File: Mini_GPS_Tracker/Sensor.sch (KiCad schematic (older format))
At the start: 15 parts

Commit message: added stm core connections
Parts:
- C14, C15, C16, C17, C18, C5, C8: renamed from C?; footprint (none) -> Capacitor_SMD:C_0805_2012Metric_Pad1.15x1.40mm_HandSolder
- R4, R5, R8: renamed from R?; footprint (none) -> Resistor_SMD:R_0805_2012Metric_Pad1.15x1.40mm_HandSolder
- Y2: renamed from Y?; footprint (none) -> Crystal:Crystal_SMD_2012-2Pin_2.0x1.2mm_HandSoldering
- gave numbers to parts that had none: 4
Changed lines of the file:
@@
 $EndDescr
 $Comp
-L Sensor_Motion:BNO055 U?
+L Sensor_Motion:BNO055 U7
 U 1 1 5E8555C8
 P 7700 3550
-F 0 "U?" H 7700 4431 50  0000 C CNN
+F 0 "U7" H 7700 4431 50  0000 C CNN
 F 1 "BNO055" H 7700 4340 50  0000 C CNN
 F 2 "Package_LGA:LGA-28_5.2x3.8mm_P0.5mm" H 7950 2900 50  0001 L CNN
@@
 	2500 6700 2500 6850
 $Comp
-L pspice:CAP C?
+L pspice:CAP C3
 U 1 1 5E6E943F
 P 3650 6350
-F 0 "C?" H 3828 6396 50  0000 L CNN
+F 0 "C3" H 3828 6396 50  0000 L CNN
 F 1 "100nF" H 3828 6305 50  0000 L CNN
 F 2 "Capacitor_SMD:C_0805_2012Metric_Pad1.15x1.40mm_HandSolder" H 3650 6350 50  0001 C CNN
@@
 $EndComp
 $Comp
-L power:+3.3V #PWR?
+L power:+3.3V #PWR0101
 U 1 1 5E6E8AC2
 P 2500 5550
-F 0 "#PWR?" H 2500 5400 50  0001 C CNN
+F 0 "#PWR0101" H 2500 5400 50  0001 C CNN
 F 1 "+3.3V" H 2515 5723 50  0000 C CNN
 F 2 "" H 2500 5550 50  0001 C CNN
@@
 $EndComp
 $Comp
-L power:GND #PWR?
+L power:GND #PWR0102
 U 1 1 5E6E7BFC
 P 2500 6950
-F 0 "#PWR?" H 2500 6700 50  0001 C CNN
+F 0 "#PWR0102" H 2500 6700 50  0001 C CNN
 F 1 "GND" H 2505 6777 50  0000 C CNN
 F 2 "" H 2500 6950 50  0001 C CNN
@@
 	1700 6400 2100 6400
 $Comp
-L Sensor_Pressure:MS5611-01BA U?
+L Sensor_Pressure:MS5611-01BA U2
 U 1 1 5E6E6D79
 P 2500 6300
-F 0 "U?" H 2830 6346 50  0000 L CNN
+F 0 "U2" H 2830 6346 50  0000 L CNN
 F 1 "MS5611-01BA" H 2830 6255 50  0000 L CNN
 F 2 "Package_LGA:LGA-8_3x5mm_P1.25mm" H 2500 6300 50  0001 C CNN
@@
 $EndComp
 $Comp
-L Sensor_Motion:ADXL343 U?
+L Sensor_Motion:ADXL343 U1
 U 1 1 5E8940BD
 P 2500 1950
-F 0 "U?" H 3044 1996 50  0000 L CNN
+F 0 "U1" H 3044 1996 50  0000 L CNN
 F 1 "ADXL343" H 3044 1905 50  0000 L CNN
 F 2 "Package_LGA:LGA-14_3x5mm_P0.8mm_LayoutBorder1x6y" H 2500 1950 50  0001 C CNN
@@
 $EndComp
 $Comp
-L power:GND #PWR?
+L power:GND #PWR0117
 U 1 1 5E8951BC
 P 2500 2950
-F 0 "#PWR?" H 2500 2700 50  0001 C CNN
+F 0 "#PWR0117" H 2500 2700 50  0001 C CNN
 F 1 "GND" H 2505 2777 50  0000 C CNN
 F 2 "" H 2500 2950 50  0001 C CNN
@@
 	1450 1850 2000 1850
 $Comp
-L pspice:CAP C?
+L pspice:CAP C5
 U 1 1 5E89F2A3
 P 3700 1950
-F 0 "C?" H 3878 1996 50  0000 L CNN
+F 0 "C5" H 3878 1996 50  0000 L CNN
 F 1 "0.1uF" H 3878 1905 50  0000 L CNN
-F 2 "" H 3700 1950 50  0001 C CNN
+F 2 "Capacitor_SMD:C_0805_2012Metric_Pad1.15x1.40mm_HandSolder" H 3700 1950 50  0001 C CNN
 F 3 "~" H 3700 1950 50  0001 C CNN
 	1    3700 1950
@@
 $EndComp
 $Comp
-L pspice:CAP C?
+L pspice:CAP C8
 U 1 1 5E89F917
 P 4200 1950
-F 0 "C?" H 4378 1996 50  0000 L CNN
+F 0 "C8" H 4378 1996 50  0000 L CNN
 F 1 "0.1uF" H 4378 1905 50  0000 L CNN
-F 2 "" H 4200 1950 50  0001 C CNN
+F 2 "Capacitor_SMD:C_0805_2012Metric_Pad1.15x1.40mm_HandSolder" H 4200 1950 50  0001 C CNN
 F 3 "~" H 4200 1950 50  0001 C CNN
 	1    4200 1950
@@
 	2500 2550 2500 2800
 $Comp
-L pspice:CAP C?
+L pspice:CAP C14
 U 1 1 5E8A3F23
 P 4700 1950
-F 0 "C?" H 4878 1996 50  0000 L CNN
+F 0 "C14" H 4878 1996 50  0000 L CNN
 F 1 "10uF" H 4878 1905 50  0000 L CNN
-F 2 "" H 4700 1950 50  0001 C CNN
+F 2 "Capacitor_SMD:C_0805_2012Metric_Pad1.15x1.40mm_HandSolder" H 4700 1950 50  0001 C CNN
 F 3 "~" H 4700 1950 50  0001 C CNN
 	1    4700 1950
@@
 NoConn ~ 2700 2450
 $Comp
-L power:GND #PWR?
+L power:GND #PWR0118
 U 1 1 5E8806F6
 P 7600 4550
-F 0 "#PWR?" H 7600 4300 50  0001 C CNN
+F 0 "#PWR0118" H 7600 4300 50  0001 C CNN
 F 1 "GND" H 7605 4377 50  0000 C CNN
 F 2 "" H 7600 4550 50  0001 C CNN
@@
 $EndComp
 $Comp
-L power:+3.3V #PWR?
+L power:+3.3V #PWR0119
 U 1 1 5E88107E
 P 7600 2350
-F 0 "#PWR?" H 7600 2200 50  0001 C CNN
+F 0 "#PWR0119" H 7600 2200 50  0001 C CNN
 F 1 "+3.3V" H 7615 2523 50  0000 C CNN
 F 2 "" H 7600 2350 50  0001 C CNN
@@
 	7600 2650 7600 2850
 $Comp
-L Device:Crystal Y?
+L Device:Crystal Y2
 U 1 1 5E883E67
 P 8600 3250
-F 0 "Y?" V 8554 3381 50  0000 L CNN
+F 0 "Y2" V 8554 3381 50  0000 L CNN
 F 1 "32.7568KHz" V 8645 3381 50  0000 L CNN
-F 2 "" H 8600 3250 50  0001 C CNN
+F 2 "Crystal:Crystal_SMD_2012-2Pin_2.0x1.2mm_HandSoldering" H 8600 3250 50  0001 C CNN
 F 3 "~" H 8600 3250 50  0001 C CNN
 	1    8600 3250
@@
 $EndComp
 $Comp
-L pspice:CAP C?
+L pspice:CAP C17
 U 1 1 5E884BB2
 P 9300 3050
-F 0 "C?" V 9615 3050 50  0000 C CNN
+F 0 "C17" V 9615 3050 50  0000 C CNN
 F 1 "22pF" V 9524 3050 50  0000 C CNN
-F 2 "" H 9300 3050 50  0001 C CNN
+F 2 "Capacitor_SMD:C_0805_2012Metric_Pad1.15x1.40mm_HandSolder" H 9300 3050 50  0001 C CNN
 F 3 "~" H 9300 3050 50  0001 C CNN
 	1    9300 3050
@@
 $EndComp
 $Comp
-L pspice:CAP C?
+L pspice:CAP C18
 U 1 1 5E886F55
 P 9300 3550
-F 0 "C?" V 8985 3550 50  0000 C CNN
+F 0 "C18" V 8985 3550 50  0000 C CNN
 F 1 "22pF" V 9076 3550 50  0000 C CNN
-F 2 "" H 9300 3550 50  0001 C CNN
+F 2 "Capacitor_SMD:C_0805_2012Metric_Pad1.15x1.40mm_HandSolder" H 9300 3550 50  0001 C CNN
 F 3 "~" H 9300 3550 50  0001 C CNN
 	1    9300 3550
@@
 $EndComp
 $Comp
-L power:GND #PWR?
+L power:GND #PWR0120
 U 1 1 5E8880AB
 P 9850 3300
-F 0 "#PWR?" H 9850 3050 50  0001 C CNN
+F 0 "#PWR0120" H 9850 3050 50  0001 C CNN
 F 1 "GND" H 9855 3127 50  0000 C CNN
 F 2 "" H 9850 3300 50  0001 C CNN
@@
 	8600 3050 9050 3050
 $Comp
-L power:GND #PWR?
+L power:GND #PWR0121
 U 1 1 5E88DCA8
 P 7000 2450
-F 0 "#PWR?" H 7000 2200 50  0001 C CNN
+F 0 "#PWR0121" H 7000 2200 50  0001 C CNN
 F 1 "GND" V 7005 2322 50  0000 R CNN
 F 2 "" H 7000 2450 50  0001 C CNN
@@
 $EndComp
 $Comp
-L pspice:CAP C?
+L pspice:CAP C15
 U 1 1 5E88E6A0
 P 7350 2450
-F 0 "C?" V 7035 2450 50  0000 C CNN
+F 0 "C15" V 7035 2450 50  0000 C CNN
 F 1 "0.1uF" V 7126 2450 50  0000 C CNN
-F 2 "" H 7350 2450 50  0001 C CNN
+F 2 "Capacitor_SMD:C_0805_2012Metric_Pad1.15x1.40mm_HandSolder" H 7350 2450 50  0001 C CNN
 F 3 "~" H 7350 2450 50  0001 C CNN
 	1    7350 2450
@@
 	7000 2450 7100 2450
 $Comp
-L Device:R R?
+L Device:R R5
 U 1 1 5E892309
 P 8650 3850
-F 0 "R?" V 8857 3850 50  0000 C CNN
+F 0 "R5" V 8857 3850 50  0000 C CNN
 F 1 "10k" V 8766 3850 50  0000 C CNN
-F 2 "" V 8580 3850 50  0001 C CNN
+F 2 "Resistor_SMD:R_0805_2012Metric_Pad1.15x1.40mm_HandSolder" V 8580 3850 50  0001 C CNN
 F 3 "~" H 8650 3850 50  0001 C CNN
 	1    8650 3850
@@
 $EndComp
 $Comp
-L Device:R R?
+L Device:R R8
 U 1 1 5E892CDB
 P 9150 3950
-F 0 "R?" V 8943 3950 50  0000 C CNN
+F 0 "R8" V 8943 3950 50  0000 C CNN
 F 1 "10k" V 9034 3950 50  0000 C CNN
-F 2 "" V 9080 3950 50  0001 C CNN
+F 2 "Resistor_SMD:R_0805_2012Metric_Pad1.15x1.40mm_HandSolder" V 9080 3950 50  0001 C CNN
 F 3 "~" H 9150 3950 50  0001 C CNN
 	1    9150 3950
@@
 $EndComp
 $Comp
-L power:GND #PWR?
+L power:GND #PWR0122
 U 1 1 5E8937EF
 P 9950 3850
-F 0 "#PWR?" H 9950 3600 50  0001 C CNN
+F 0 "#PWR0122" H 9950 3600 50  0001 C CNN
 F 1 "GND" V 9955 3722 50  0000 R CNN
 F 2 "" H 9950 3850 50  0001 C CNN
@@
 $EndComp
 $Comp
-L power:GND #PWR?
+L power:GND #PWR0123
 U 1 1 5E894898
 P 9950 3950
-F 0 "#PWR?" H 9950 3700 50  0001 C CNN
+F 0 "#PWR0123" H 9950 3700 50  0001 C CNN
 F 1 "GND" V 9955 3822 50  0000 R CNN
 F 2 "" H 9950 3950 50  0001 C CNN
@@
 $EndComp
 $Comp
-L pspice:CAP C?
+L pspice:CAP C16
 U 1 1 5E8959B0
 P 8550 4450
-F 0 "C?" V 8235 4450 50  0000 C CNN
+F 0 "C16" V 8235 4450 50  0000 C CNN
 F 1 "0.1uF" V 8326 4450 50  0000 C CNN
-F 2 "" H 8550 4450 50  0001 C CNN
+F 2 "Capacitor_SMD:C_0805_2012Metric_Pad1.15x1.40mm_HandSolder" H 8550 4450 50  0001 C CNN
 F 3 "~" H 8550 4450 50  0001 C CNN
 	1    8550 4450
@@
 $EndComp
 $Comp
-L power:GND #PWR?
+L power:GND #PWR0124
 U 1 1 5E89C6D8
 P 8550 4800
-F 0 "#PWR?" H 8550 4550 50  0001 C CNN
+F 0 "#PWR0124" H 8550 4550 50  0001 C CNN
 F 1 "GND" V 8555 4672 50  0000 R CNN
 F 2 "" H 8550 4800 50  0001 C CNN
@@
 	8550 4050 8550 4200
 $Comp
-L Device:R R?
+L Device:R R4
 U 1 1 5E897EFC
 P 6950 4300
-F 0 "R?" H 7020 4346 50  0000 L CNN
+F 0 "R4" H 7020 4346 50  0000 L CNN
 F 1 "10K" H 7020 4255 50  0000 L CNN
-F 2 "" V 6880 4300 50  0001 C CNN
+F 2 "Resistor_SMD:R_0805_2012Metric_Pad1.15x1.40mm_HandSolder" V 6880 4300 50  0001 C CNN
 F 3 "~" H 6950 4300 50  0001 C CNN
 	1    6950 4300
@@
 $EndComp
 $Comp
-L power:GND #PWR?
+L power:GND #PWR0125
 U 1 1 5E898E99
 P 6950 4550
-F 0 "#PWR?" H 6950 4300 50  0001 C CNN
+F 0 "#PWR0125" H 6950 4300 50  0001 C CNN
 F 1 "GND" H 6955 4377 50  0000 C CNN
 F 2 "" H 6950 4550 50  0001 C CNN
@@
 $EndComp
 $Comp
-L power:GND #PWR?
+L power:GND #PWR0126
 U 1 1 5E89968D
 P 6600 4550
-F 0 "#PWR?" H 6600 4300 50  0001 C CNN
+F 0 "#PWR0126" H 6600 4300 50  0001 C CNN
 F 1 "GND" H 6605 4377 50  0000 C CNN
 F 2 "" H 6600 4550 50  0001 C CNN
@@
 	6550 3850 7100 3850
 $Comp
-L power:GND #PWR?
+L power:GND #PWR0127
 U 1 1 5E8A27A4
 P 5500 3550
-F 0 "#PWR?" H 5500 3300 50  0001 C CNN
+F 0 "#PWR0127" H 5500 3300 50  0001 C CNN
 F 1 "GND" H 5505 3377 50  0000 C CNN
 F 2 "" H 5500 3550 50  0001 C CNN
@@
 $EndComp
 $Comp
-L power:+3.3V #PWR?
+L power:+3.3V #PWR0128
 U 1 1 5E8A32E9
 P 5500 3450
-F 0 "#PWR?" H 5500 3300 50  0001 C CNN
+F 0 "#PWR0128" H 5500 3300 50  0001 C CNN
 F 1 "+3.3V" H 5515 3623 50  0000 C CNN
 F 2 "" H 5500 3450 50  0001 C CNN

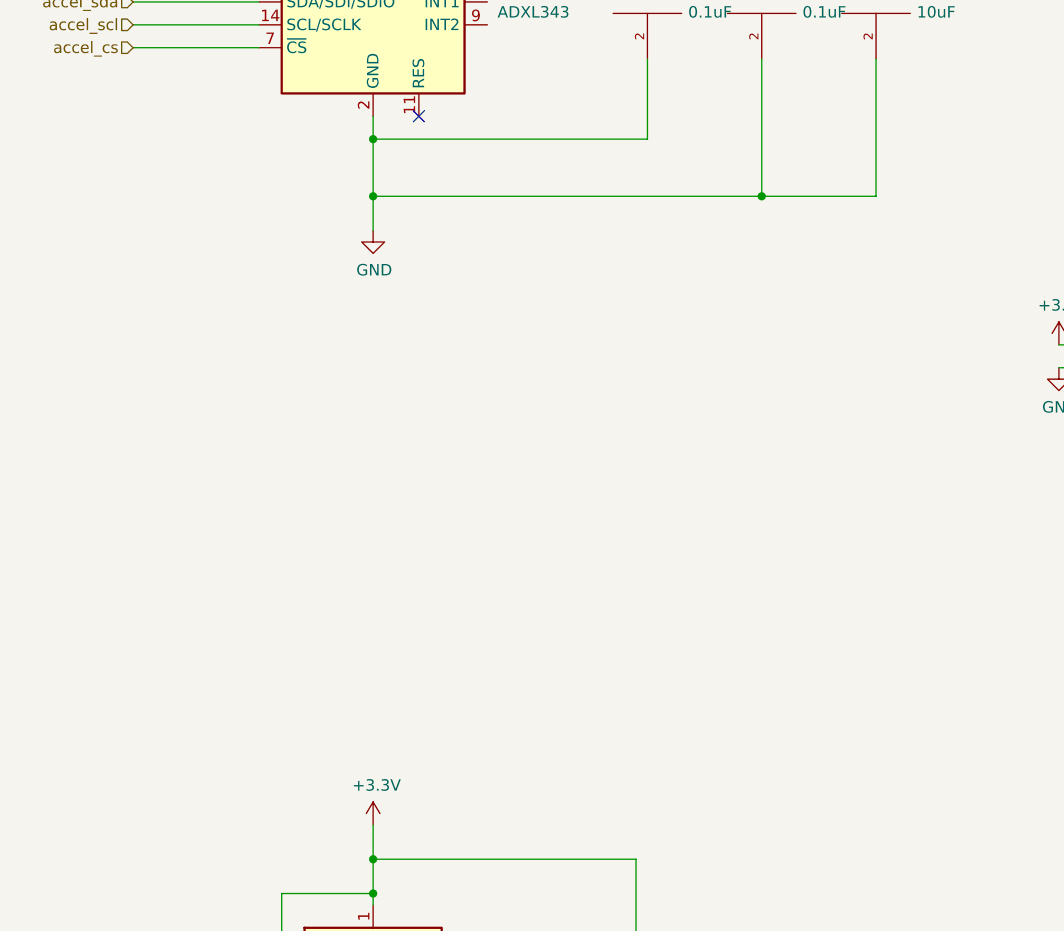
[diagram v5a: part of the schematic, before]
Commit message: Add files via upload
Making update for 100 pin CPU
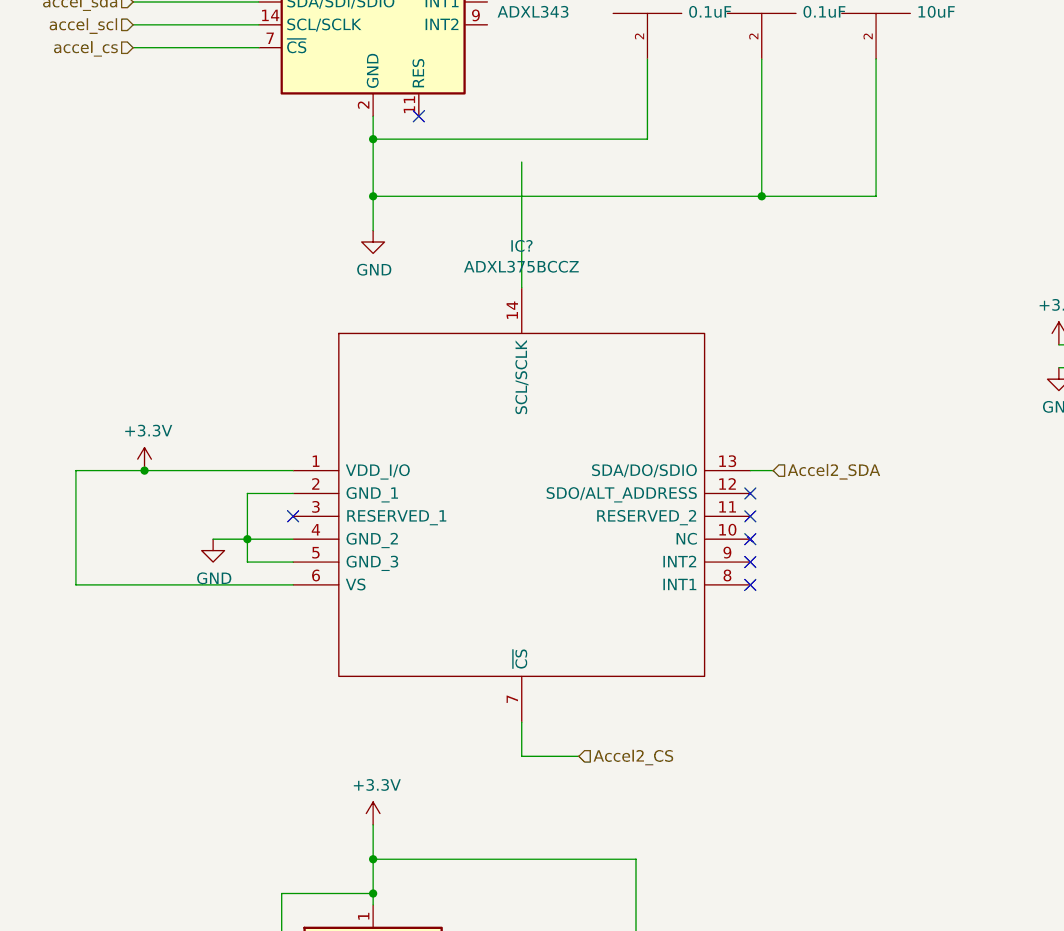
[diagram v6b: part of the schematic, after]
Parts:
- added IC?: ADXL375BCCZ, CC-14-1, symbol SamacSys_Parts:ADXL375BCCZ
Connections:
- net +3V3: now also IC?.1 (VDD_I/O), IC?.6 (VS)
- net GND: now also IC?.2 (GND_1), IC?.4 (GND_2), IC?.5 (GND_3)
- new net Accel2_CS: IC?.7 (~CS)
- new net Accel2_SDA: IC?.13 (SDA/DO/SDIO)
- no-connect marks 4 -> 10
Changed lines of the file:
@@
 EESchema Schematic File Version 4
+LIBS:Mini_GPS_Tracker-cache
 EELAYER 30 0
 EELAYER END
 $Descr A4 11693 8268
 encoding utf-8
-Sheet 2 11
+Sheet 2 7
 Title ""
 Date ""
@@
 Wire Wire Line
 	7100 3550 5500 3550
+Text HLabel 4250 4000 2    50   Input ~ 0
+Accel2_SDA
+Wire Wire Line
+	4250 4000 4150 4000
+$Comp
+L SamacSys_Parts:ADXL375BCCZ IC?
+U 1 1 5EB47FDF
+P 2150 4000
+AR Path="/5E9E34E6/5EB47FDF" Ref="IC?"  Part="1"
+AR Path="/5E70BD5E/5EB47FDF" Ref="IC?"  Part="1"
+F 0 "IC?" H 3150 4981 50  0000 C CNN
+F 1 "ADXL375BCCZ" H 3150 4890 50  0000 C CNN
+F 2 "CC-14-1" H 4000 4600 50  0001 L CNN
+F 3 "https://componentsearchengine.com/Datasheets/1/ADXL375BCCZ.pdf" H 4000 4500 50  0001 L CNN
+F 4 "ADXL375BCCZ Analog Devices, 3-Axis Accelerometer, I2C, Serial-3 Wire, Serial-4 Wire, Serial-SPI, 14-Pin LGA" H 4000 4400 50  0001 L CNN "Description"
+F 5 "" H 4000 4300 50  0001 L CNN "Height"
+F 6 "584-ADXL375BCCZ" H 4000 4200 50  0001 L CNN "Mouser Part Number"
+F 7 "https://www.mouser.com/Search/Refine.aspx?Keyword=584-ADXL375BCCZ" H 4000 4100 50  0001 L CNN "Mouser Price/Stock"
+F 8 "Analog Devices" H 4000 4000 50  0001 L CNN "Manufacturer_Name"
+F 9 "ADXL375BCCZ" H 4000 3900 50  0001 L CNN "Manufacturer_Part_Number"
+	1    2150 4000
+	1    0    0    -1
+$EndComp
+Wire Wire Line
+	3150 2650 3150 3200
+Wire Wire Line
+	2150 4100 1950 4100
+Wire Wire Line
+	1950 4100 1950 4300
+Wire Wire Line
+	1950 4400 2150 4400
+Wire Wire Line
+	1950 4300 2150 4300
+Connection ~ 1950 4300
+Wire Wire Line
+	1950 4300 1950 4400
+$Comp
+L power:GND #PWR?
+U 1 1 5EB47FEC
+P 1800 4300
+AR Path="/5E9E34E6/5EB47FEC" Ref="#PWR?"  Part="1"
+AR Path="/5E70BD5E/5EB47FEC" Ref="#PWR?"  Part="1"
+F 0 "#PWR?" H 1800 4050 50  0001 C CNN
+F 1 "GND" H 1805 4127 50  0000 C CNN
+F 2 "" H 1800 4300 50  0001 C CNN
+F 3 "" H 1800 4300 50  0001 C CNN
+	1    1800 4300
+	1    0    0    -1
+$EndComp
+Wire Wire Line
+	1800 4300 1950 4300
+Wire Wire Line
+	2150 4000 1500 4000
+Wire Wire Line
+	1200 4000 1200 4500
+Wire Wire Line
+	1200 4500 2150 4500
+$Comp
+L power:+3.3V #PWR?
+U 1 1 5EB47FF6
+P 1500 4000
+AR Path="/5E9E34E6/5EB47FF6" Ref="#PWR?"  Part="1"
+AR Path="/5E70BD5E/5EB47FF6" Ref="#PWR?"  Part="1"
+F 0 "#PWR?" H 1500 3850 50  0001 C CNN
+F 1 "+3.3V" H 1515 4173 50  0000 C CNN
+F 2 "" H 1500 4000 50  0001 C CNN
+F 3 "" H 1500 4000 50  0001 C CNN
+	1    1500 4000
+	1    0    0    -1
+$EndComp
+Connection ~ 1500 4000
+Wire Wire Line
+	1500 4000 1200 4000
+NoConn ~ 4150 4300
+NoConn ~ 4150 4400
+NoConn ~ 4150 4500
+NoConn ~ 2150 4200
+Text HLabel 3400 5250 2    50   Input ~ 0
+Accel2_CS
+Wire Wire Line
+	3150 5100 3150 5250
+Wire Wire Line
+	3150 5250 3400 5250
+NoConn ~ 4150 4100
+NoConn ~ 4150 4200
 $EndSCHEMATC
